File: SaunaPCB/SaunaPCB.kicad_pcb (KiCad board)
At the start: 2 copper layers, 200 x 110 mm, 65 parts, among them J201 KL3RM7.62, J202 KL3RM7.62, J203 KL3RM7.62, J204 KL2RM5.08, J205 KL3RM7.62, J206 KL3RM7.62, J301 KL2RM5.08, J302 KL2RM5.08, J303 KL2RM5.08, J304 KL2RM5.08, K201 Relais_SPDT_CO, K202 Relais_SPDT_CO, K203 Relais_SPDT_CO, K204 Relais_SPDT_CO, K205 Relais_SPDT_CO, K206 Relais_SPDT_CO, K207 Relais_SPDT_CO, U201 LHE05-20B24, U202 4N25, U203 4N25, U204 4N25, U301 ESP32-DEVKITC, U302 LM2576T-5

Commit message: some step files added
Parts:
- moved J310 36.2 mm to (252.1, 143.1), turned to 0 degrees
- moved J307 32.4 mm to (217.8, 143.1), turned to 0 degrees
- moved J309 13.3 mm to (240.6, 143.1), turned to 0 degrees
- moved J308 9.57 mm to (229.2, 143.1), turned to 0 degrees
- moved J304 8.02 mm to (162.6, 49.5), turned to 180 degrees
- renumbered C201 to C301, C202 to C302, C203 to C303, C204 to C304, C205 to C305, D201 to D301, D202 to D302, D301 to D303, D203 to D304, D204 to D305, D205 to D306, D206 to D307, D207 to D308, F201 to F301, H201 to H301, H202 to H302, H203 to H303, H204 to H304, H205 to H305, J201 to J301, J202 to J302, J203 to J303, J204 to J304, J205 to J305, J206 to J306, J301 to J307, J302 to J308, J303 to J309, J304 to J310, K201 to K301, K202 to K302, K203 to K303, K204 to K304, K205 to K305, K206 to K306, K207 to K307, L201 to L301, L202 to L302, L301 to L303, L203 to L304, R201 to R301, R202 to R302, R203 to R303, R204 to R304, R205 to R305, R206 to R306, R207 to R307, R208 to R308, R209 to R309, R210 to R310, R211 to R311, R212 to R312, R213 to R313, R301 to R314, R302 to R315, R303 to R316, R306 to R317, R304 to R318, R305 to R319, U201 to U301, U202 to U303, U203 to U304, U204 to U305, U301 to U306

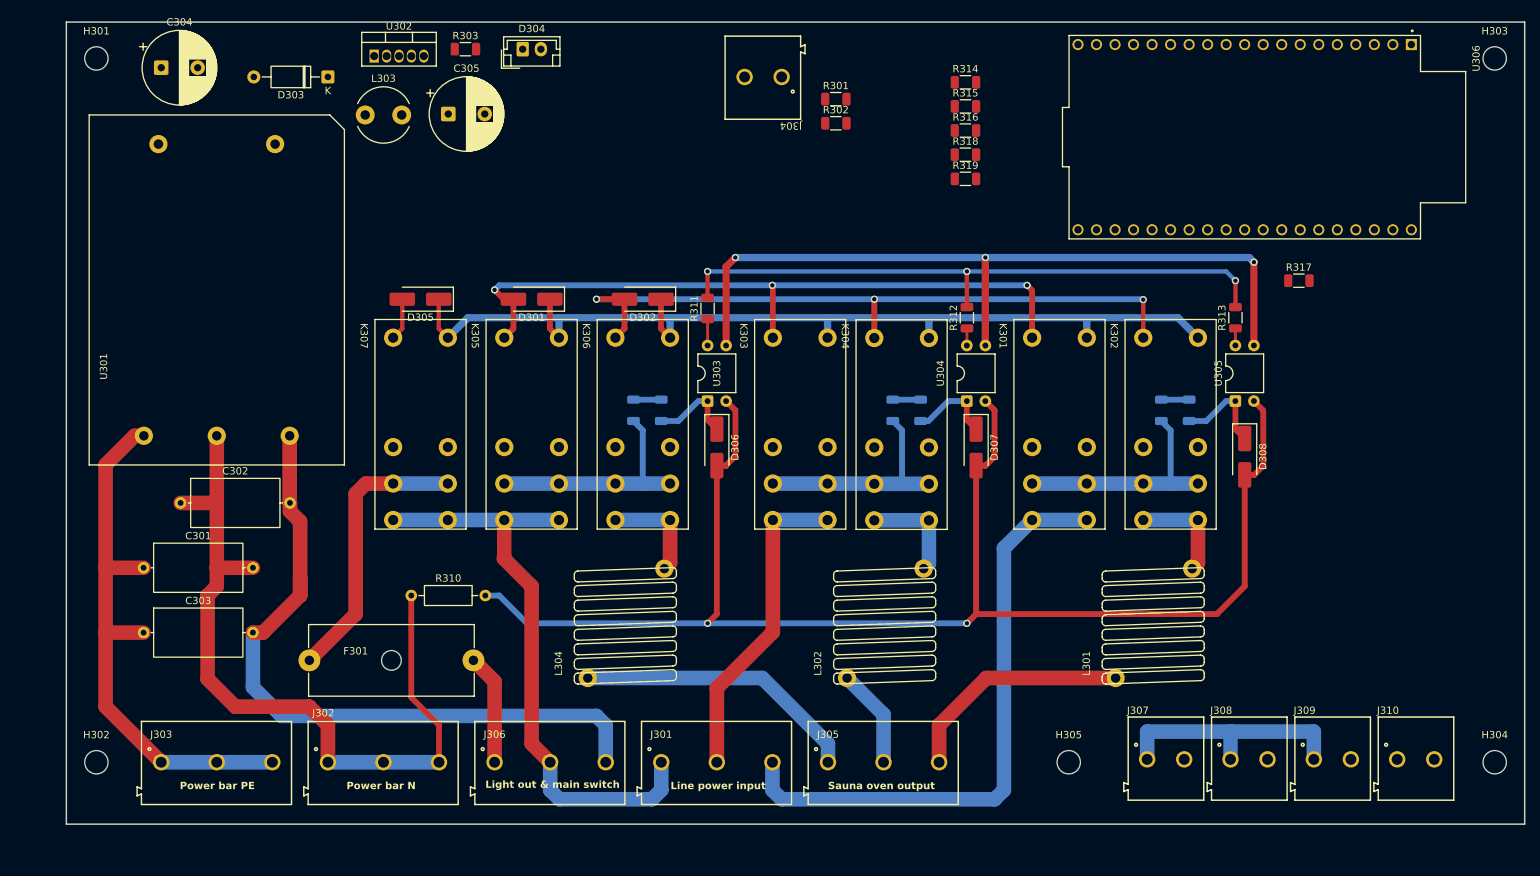
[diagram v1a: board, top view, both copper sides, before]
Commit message: Hall sensors for current measurement added
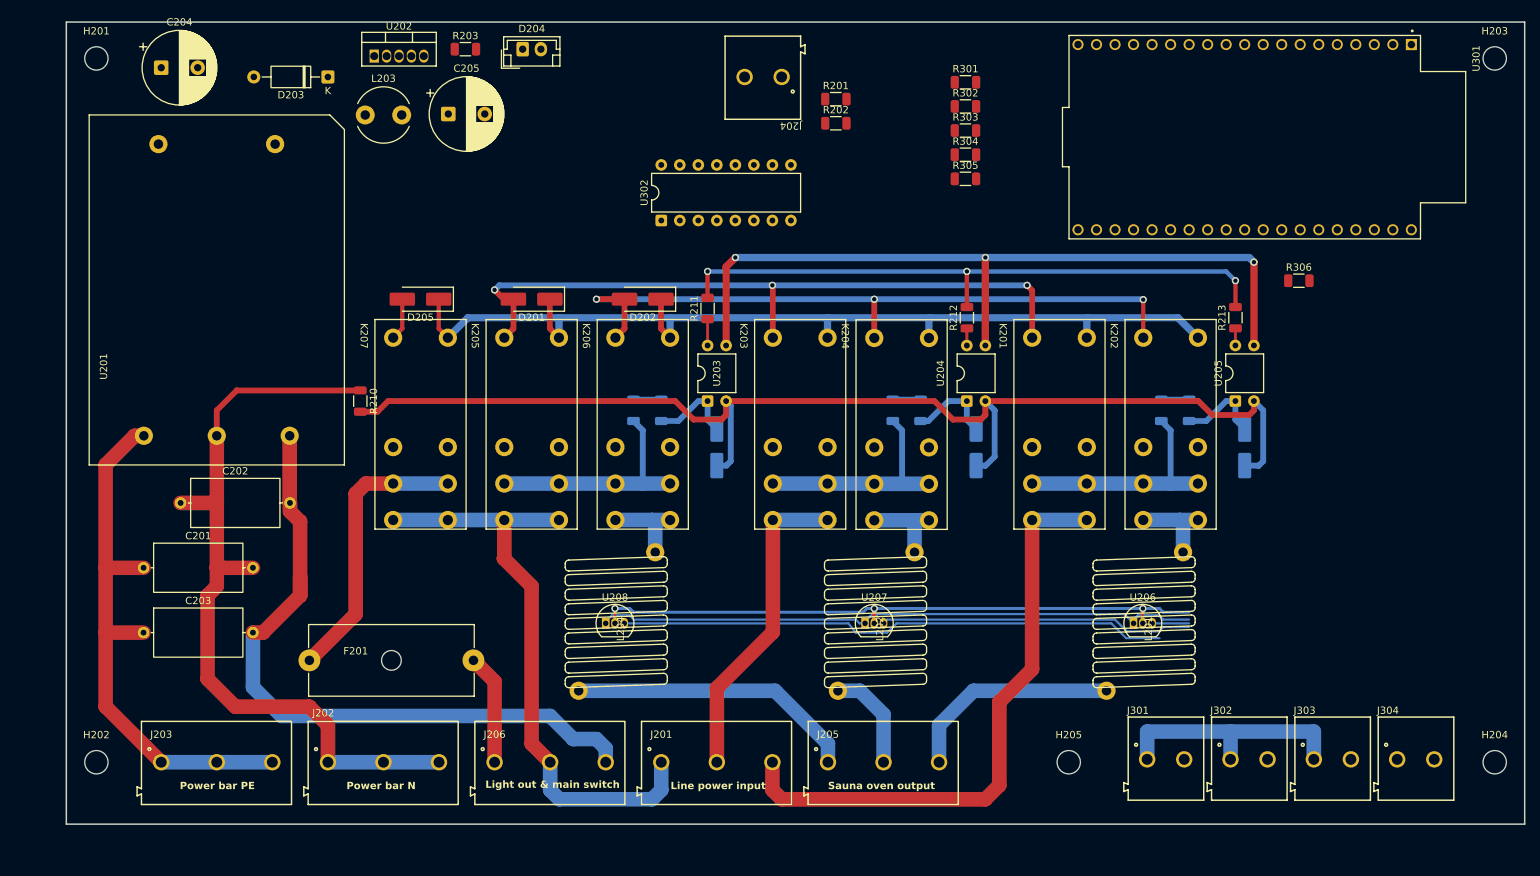
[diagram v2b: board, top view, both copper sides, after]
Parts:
- added U206: DRV5033AJxLPG, Package_TO_SOT_THT:TO-92_Inline, F.Cu at (213.4, 124.5)
- added U207: DRV5033AJxLPG, Package_TO_SOT_THT:TO-92_Inline, F.Cu at (176.5, 124.5)
- added U208: DRV5033AJxLPG, Package_TO_SOT_THT:TO-92_Inline, F.Cu at (141.0, 124.5)
- added U302: ULN2003, Package_DIP:DIP-16_W7.62mm, F.Cu at (148.6, 69.2)
- D206: renamed from D306; moved to B.Cu
- D207: renamed from D307; moved to B.Cu
- D208: renamed from D308; moved to B.Cu
- L201: renamed from L301; footprint SaunaProject:Current_Coil_15X14 -> SaunaProject:Current_Coil_19X14
- L202: renamed from L302; footprint SaunaProject:Current_Coil_15X14 -> SaunaProject:Current_Coil_19X14
- L204: renamed from L304; footprint SaunaProject:Current_Coil_15X14 -> SaunaProject:Current_Coil_19X14
- R210: renamed from R310; footprint Resistor_THT:R_Axial_DIN0207_L6.3mm_D2.5mm_P10.16mm_Horizontal -> Resistor_SMD:R_1206_3216Metric
- moved R210 27.6 mm to (107.3, 94.0), turned to -90 degrees
- moved D208 1.27 mm to (228.6, 100.3)
- renumbered C301 to C201, C302 to C202, C303 to C203, C304 to C204, C305 to C205, D301 to D201, D302 to D202, D303 to D203, D304 to D204, D305 to D205, F301 to F201, H301 to H201, H302 to H202, H303 to H203, H304 to H204, H305 to H205, J301 to J201, J302 to J202, J303 to J203, J304 to J204, J305 to J205, J306 to J206, J307 to J301, J308 to J302, J309 to J303, J310 to J304, K301 to K201, K302 to K202, K303 to K203, K304 to K204, K305 to K205, K306 to K206, K307 to K207, L303 to L203, R301 to R201, R302 to R202, R303 to R203, R304 to R204, R305 to R205, R306 to R206, R307 to R207, R308 to R208, R309 to R209, R311 to R211, R312 to R212, R313 to R213, R314 to R301, R315 to R302, R316 to R303, R318 to R304, R319 to R305, R317 to R306, U301 to U201, U302 to U202, U303 to U203, U304 to U204, U305 to U205, U306 to U301
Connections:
- net /Power distribution part/Light_Out renamed Net-(F201-Pad1)
- net Net-(F301-Pad2) renamed Light_out
- U301 pad 10: Relais_1 -> /Controller part/R1_3V3
- U301 pad 11: Relais_2 -> /Controller part/R2_3V3
- U301 pad 12: Relais_3 -> /Controller part/R3_3V3
- U301 pad 31: LCD_BACKLIGHT -> /Controller part/LCDBL_3V3
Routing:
- net GND: track 141.8 -> 227.2 mm, vias 3 -> 6
- net +3V3: track 85.0 -> 168.3 mm
- net I_L1: track 0.00 -> 75.4 mm
- net I_L2: track 0.00 -> 43.1 mm
- net Net-(D206-A): track 200.6 -> 165.4 mm, vias 2 -> 0
- net I_L3: track 0.00 -> 5.08 mm
- net /Power distribution part/K206_Out: track 14.5 -> 12.1 mm
- net /Power distribution part/K202_Out: track 14.5 -> 12.1 mm
- net /Power distribution part/K204_Out: track 14.4 -> 12.1 mm
- net /Power distribution part/L3_OUT: track 32.0 -> 30.0 mm
- net L1_ON: track 96.7 -> 94.9 mm
- net Net-(D208-K): track 13.1 -> 11.9 mm
- net L3: track 82.7 -> 82.0 mm
- net /Power distribution part/L2_OUT: track 13.6 -> 14.1 mm
- net /Power distribution part/L1_OUT: track 39.2 -> 39.7 mm

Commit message: First routing almost finished Connector to LCD and encoder to be added!
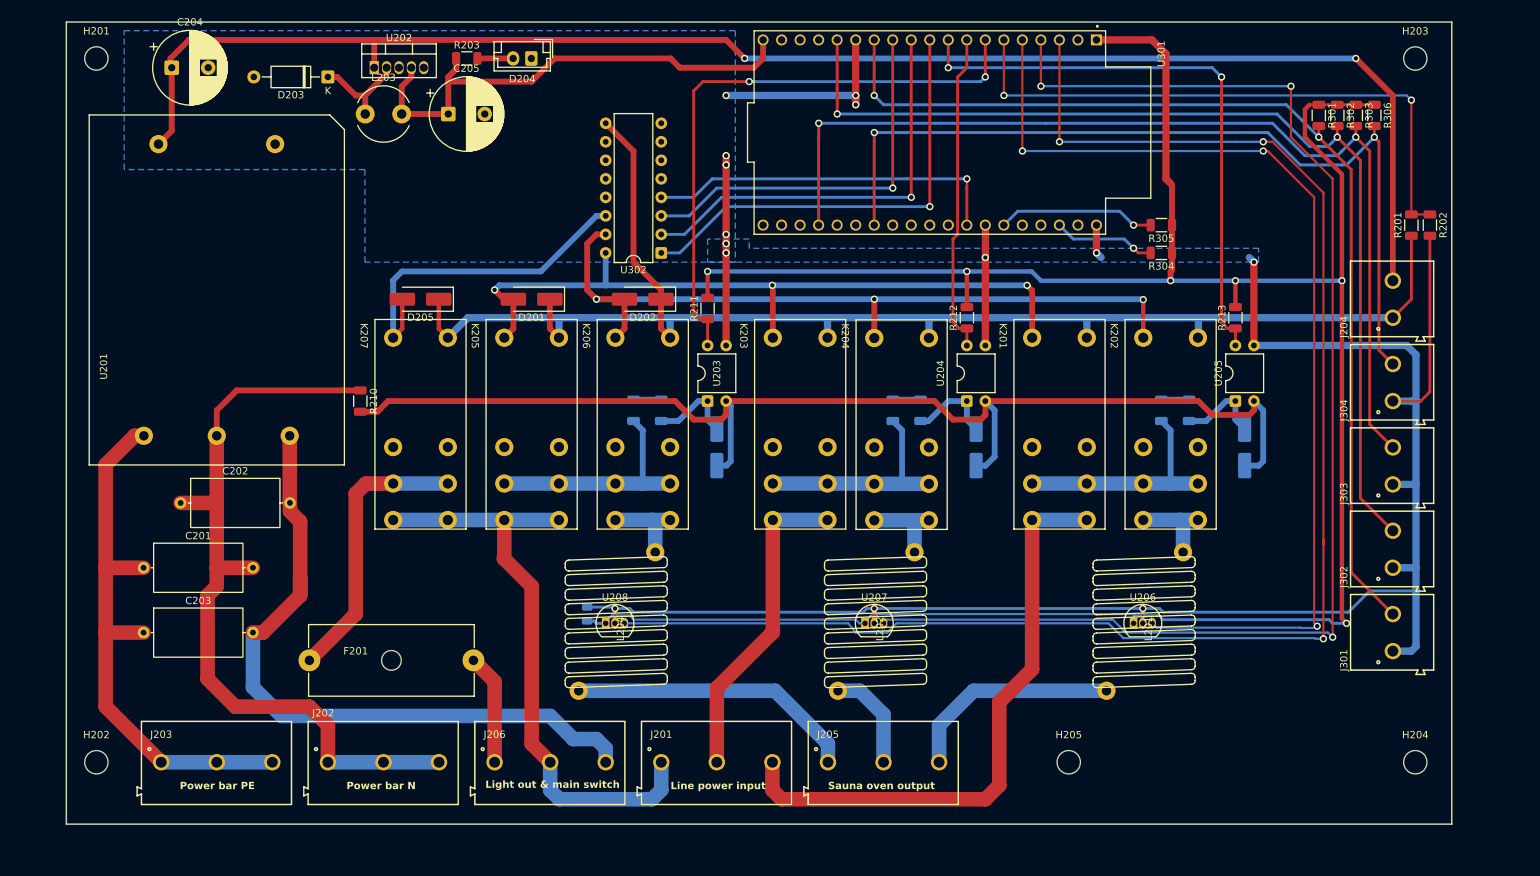
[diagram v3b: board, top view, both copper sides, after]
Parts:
- added C206: 100nF, Capacitor_SMD:C_0805_2012Metric, B.Cu at (138.4, 123.2)
- U206, U207, U208: value DRV5033AJxLPG -> DRV5053
- moved J204 91.6 mm to (248.9, 80.0), turned to 90 degrees
- moved R202 82.7 mm to (254.0, 69.8), turned to -90 degrees
- moved R201 80.8 mm to (251.5, 69.8), turned to 90 degrees
- moved R303 53.6 mm to (243.8, 54.8), turned to -90 degrees
- moved J304 51.8 mm to (248.9, 91.4), turned to 90 degrees
- moved R302 51.0 mm to (241.3, 54.8), turned to -90 degrees
- moved R301 48.7 mm to (238.8, 54.8), turned to -90 degrees
- moved U301 43.2 mm to (185.4, 57.1)
- moved J303 41.1 mm to (248.9, 102.9), turned to 90 degrees
- moved J301 35.7 mm to (248.9, 125.7), turned to 90 degrees
- moved J302 34.9 mm to (248.9, 114.3), turned to 90 degrees
- moved R304 30.1 mm to (217.2, 73.7), turned to 180 degrees
- moved R305 27.6 mm to (217.2, 69.8), turned to 180 degrees
- moved R306 24.9 mm to (246.4, 54.8), turned to -90 degrees
- moved H203 10.9 mm to (252.0, 47.0)
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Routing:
- net +24V: track 0.00 -> 213.6 mm, vias 0 -> 2
- net +3V3: track 168.3 -> 331.9 mm, vias 3 -> 6
- net Light_OnOff: track 0.00 -> 142.1 mm, vias 0 -> 2
- net Standby_OnOff: track 0.00 -> 139.8 mm, vias 0 -> 2
- net I_L2: track 43.1 -> 181.4 mm, vias 0 -> 3
- net I_L1: track 75.4 -> 213.4 mm, vias 0 -> 3
- net Door_Contact: track 0.00 -> 136.7 mm, vias 0 -> 2
- net I_L3: track 5.08 -> 139.9 mm, vias 0 -> 3
- net KTY_Sensor: track 0.00 -> 118.4 mm, vias 0 -> 2
- net GND: track 227.2 -> 311.9 mm, vias 6 -> 14
- net 24V_FB: track 0.00 -> 82.0 mm, vias 0 -> 2
- net L1_Sense: track 3.62 -> 82.2 mm, vias 0 -> 2
- net L3_Sense: track 2.34 -> 80.1 mm, vias 0 -> 2
- net +5V: track 0.00 -> 69.4 mm
- net 24VR: track 136.4 -> 204.3 mm
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- added copper zone on B.Cu, net GND
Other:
- board size 200 x 110 mm -> 190 x 110 mm

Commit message: Connector to LCD and decoder added
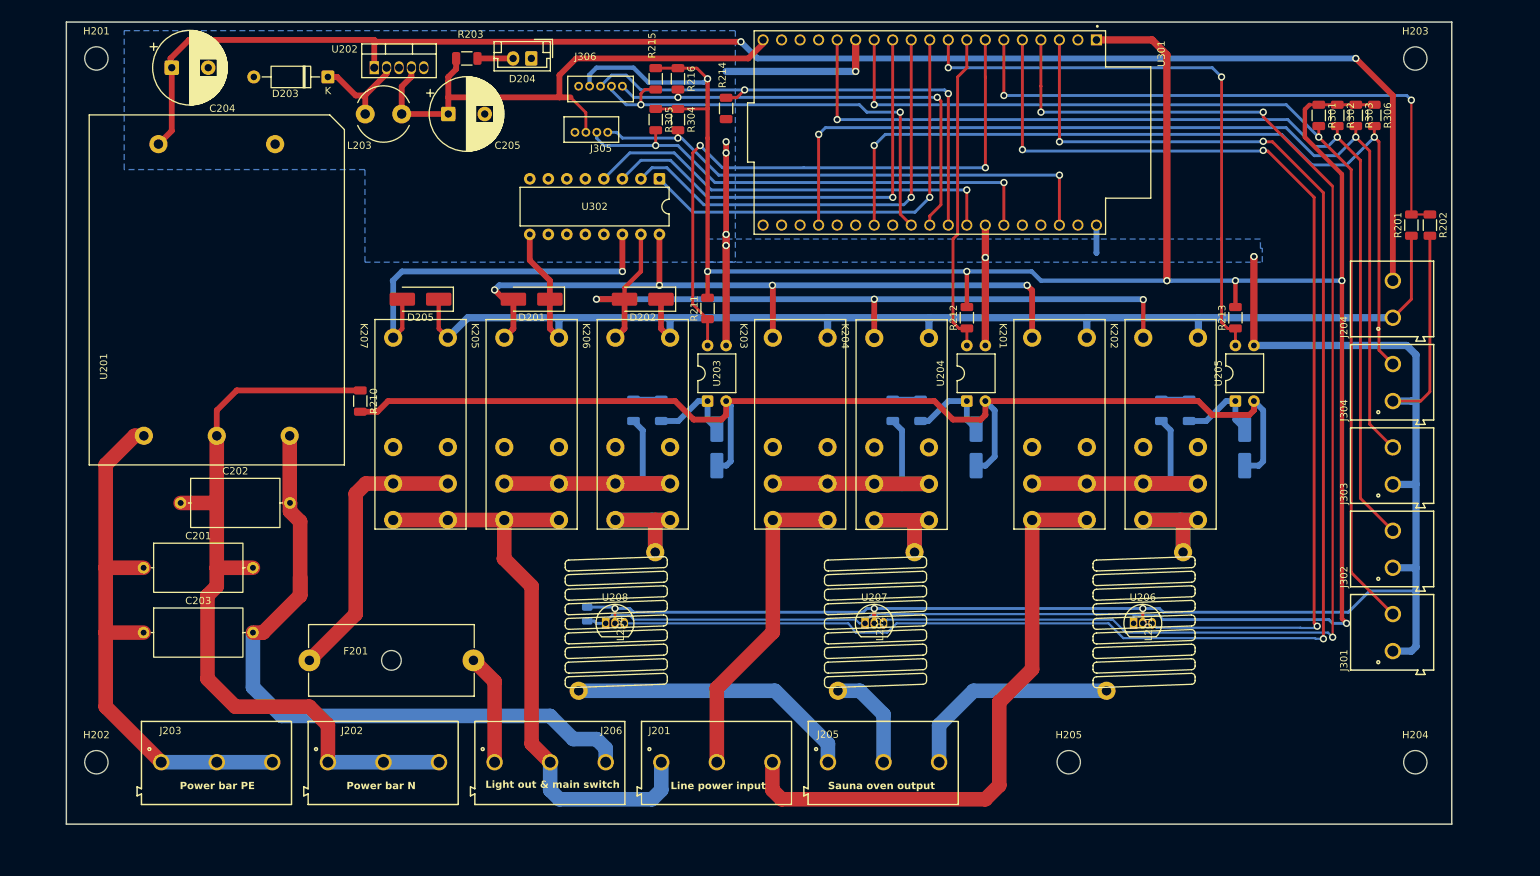
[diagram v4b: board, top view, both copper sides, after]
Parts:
- added J305: B4B-ZR, MyConnectors:B4B-ZR, F.Cu at (142.7, 58.4)
- added J306: B5B-ZR, MyConnectors:B5B-ZR, F.Cu at (135.8, 49.5)
- added R214: 2K2, Resistor_SMD:R_1206_3216Metric, F.Cu at (157.5, 53.8)
- added R215: 10K, Resistor_SMD:R_1206_3216Metric, F.Cu at (147.8, 49.8)
- added R216: 10K, Resistor_SMD:R_1206_3216Metric, F.Cu at (150.9, 49.8)
- moved R305 70.8 mm to (147.8, 55.4), turned to -90 degrees
- moved R304 68.8 mm to (150.9, 55.4), turned to -90 degrees
- moved U302 10.2 mm to (148.3, 63.5), turned to -90 degrees
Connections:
- net LCD_SCL renamed SCL
- net LCD_SDA renamed SDA
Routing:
- net ENC_SWITCH: track 0.00 -> 70.4 mm, vias 0 -> 2
- net ENC_CLK: track 0.00 -> 63.3 mm, vias 0 -> 2
- net ENC_DT: track 0.00 -> 61.3 mm, vias 0 -> 2
- net +3V3: track 331.9 -> 392.1 mm, vias 6 -> 7
- net SCL: track 14.1 -> 72.6 mm, vias 1 -> 2
- net SDA: track 21.7 -> 67.2 mm, vias 1 -> 2
- net 24VR: track 204.3 -> 187.1 mm
- net /Power distribution part/K202_Out: track 12.1 -> 24.1 mm
- net /Power distribution part/K206_Out: track 12.1 -> 24.1 mm
- net /Power distribution part/K204_Out: track 12.1 -> 24.0 mm
- net /Controller part/LCDBL_3V3: track 49.3 -> 58.2 mm
- net /Controller part/R3_3V3: track 53.7 -> 61.8 mm
- net +5V: track 69.4 -> 77.1 mm
- net /Power distribution part/L2_SW: track 30.6 -> 38.1 mm
- net /Power distribution part/L3_SW: track 31.8 -> 39.3 mm
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
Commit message: Usage ULN changed Top silkscreen PCB almost ready Values Diodes changed all 1N4004 => SG1 Relay diodes changed from NB to used (for security reasons; Diode in ULN may be not powerful enough)
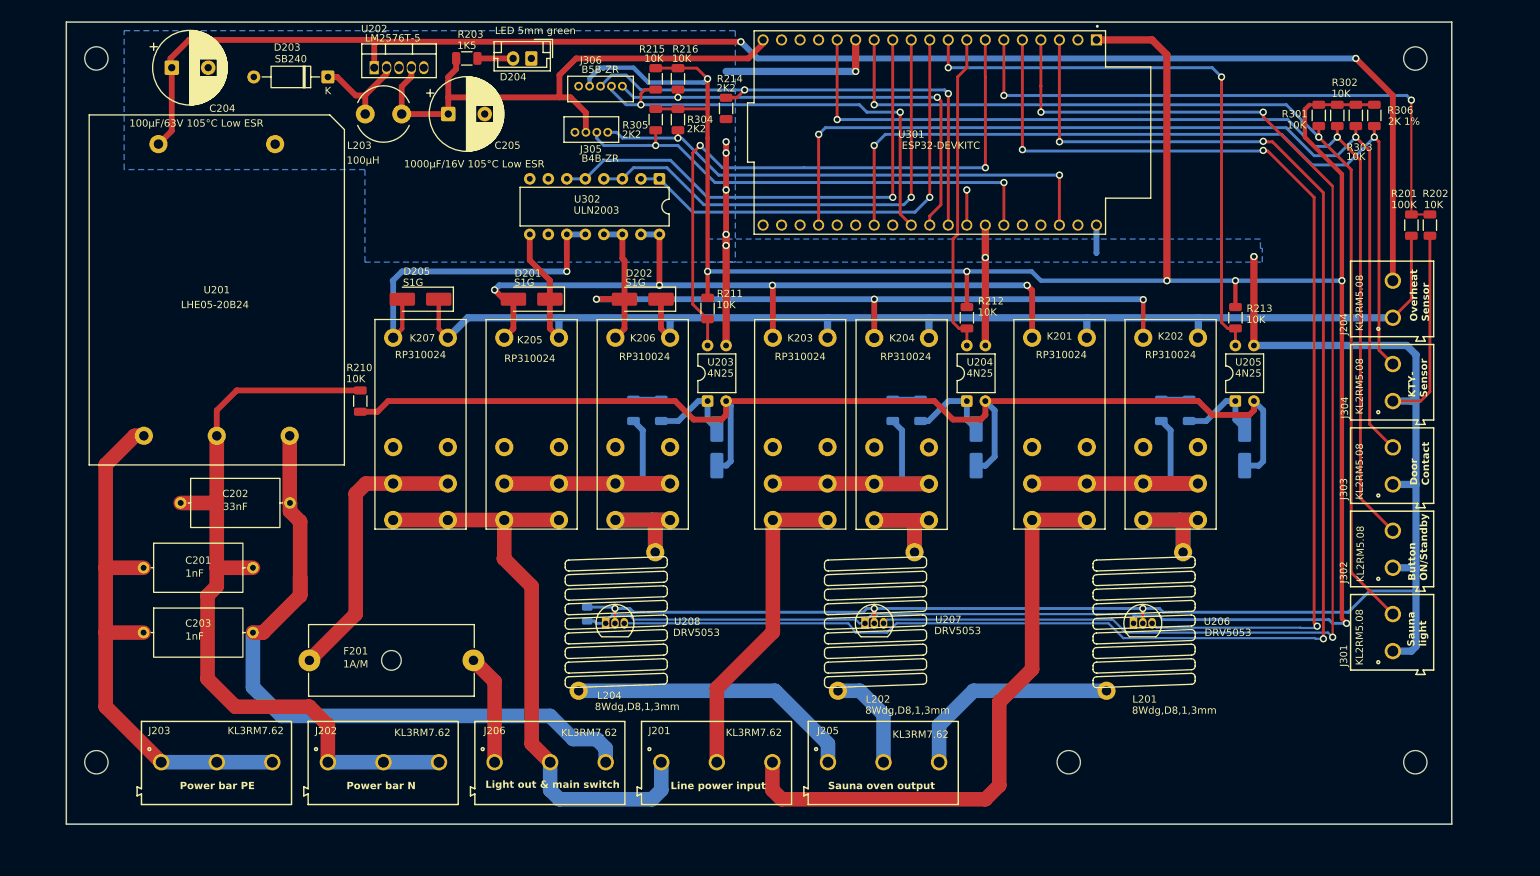
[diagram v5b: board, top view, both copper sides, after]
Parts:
- D201, D202, D205, D206, D207, D208: value 1N4004 -> S1G
- D204: value LED -> LED 5mm green
- K201, K202, K203, K204, K205, K206, K207: value Relais_SPDT_CO -> RP310024
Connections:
- U302 pad 11: unconnected-(U302-O6-Pad11) -> Relais_3
- U302 pad 12: unconnected-(U302-O5-Pad12) -> Relais_3
- U302 pad 13: LCD_BACKLIGHT -> Relais_2
- U302 pad 14: Relais_3 -> Relais_2
- U302 pad 15: Relais_2 -> Relais_1
- U302 pad 2: /Controller part/R2_3V3 -> /Controller part/R1_3V3
- U302 pad 3: /Controller part/R3_3V3 -> /Controller part/R2_3V3
- U302 pad 4: /Controller part/LCDBL_3V3 -> /Controller part/R2_3V3
- U302 pad 5: unconnected-(U302-I5-Pad5) -> /Controller part/R3_3V3
- U302 pad 6: unconnected-(U302-I6-Pad6) -> /Controller part/R3_3V3
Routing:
- net /Controller part/LCDBL_3V3: track 58.2 -> 4.83 mm
- net /Controller part/R3_3V3: track 61.8 -> 69.5 mm
- net Relais_3: track 50.7 -> 45.7 mm
- net /Controller part/R2_3V3: track 61.8 -> 66.9 mm
- net Relais_1: track 103.9 -> 106.4 mm
- net /Controller part/R1_3V3: track 61.4 -> 63.9 mm
- net Relais_2: track 105.0 -> 106.8 mm
- net GND: vias 10 -> 11
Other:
- board text added: "Button ON/Standby"
- board text added: "Door Contact"
- board text added: "KTY- Sensor"
- board text added: "Overheat Sensor"
- board text added: "Sauna light"
